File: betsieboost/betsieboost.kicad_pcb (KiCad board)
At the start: 2 copper layers, 35.8 x 14.2 mm, 10 parts, among them J1 Conn_01x03_Male, U1 XL6019E1

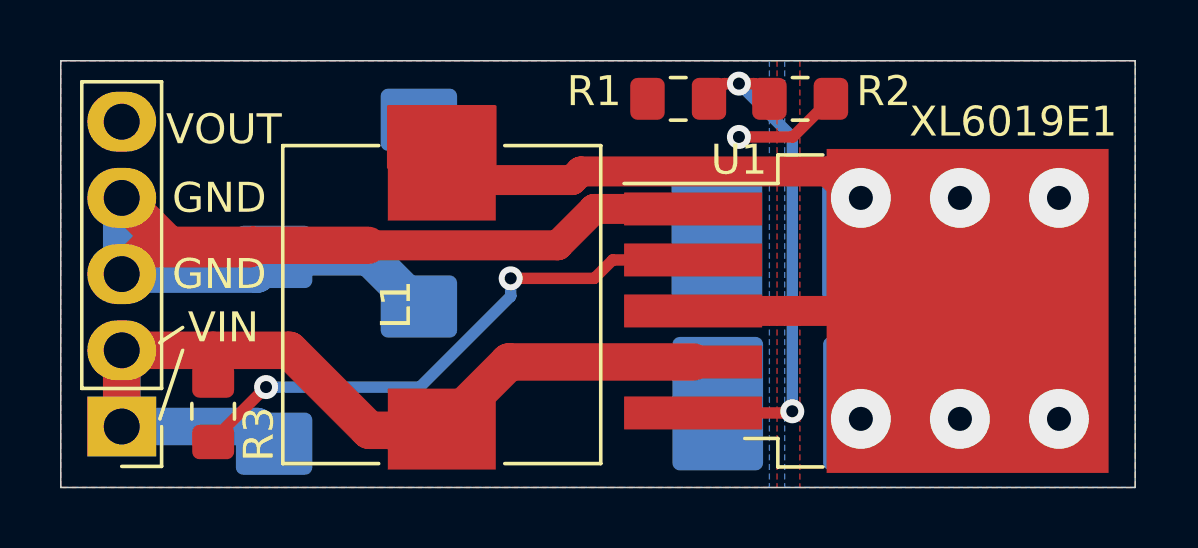
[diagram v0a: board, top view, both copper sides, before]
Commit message: This was an update to add a ceramic cap to the output because those tants do not work well. but I did not respin the board I just hacked it
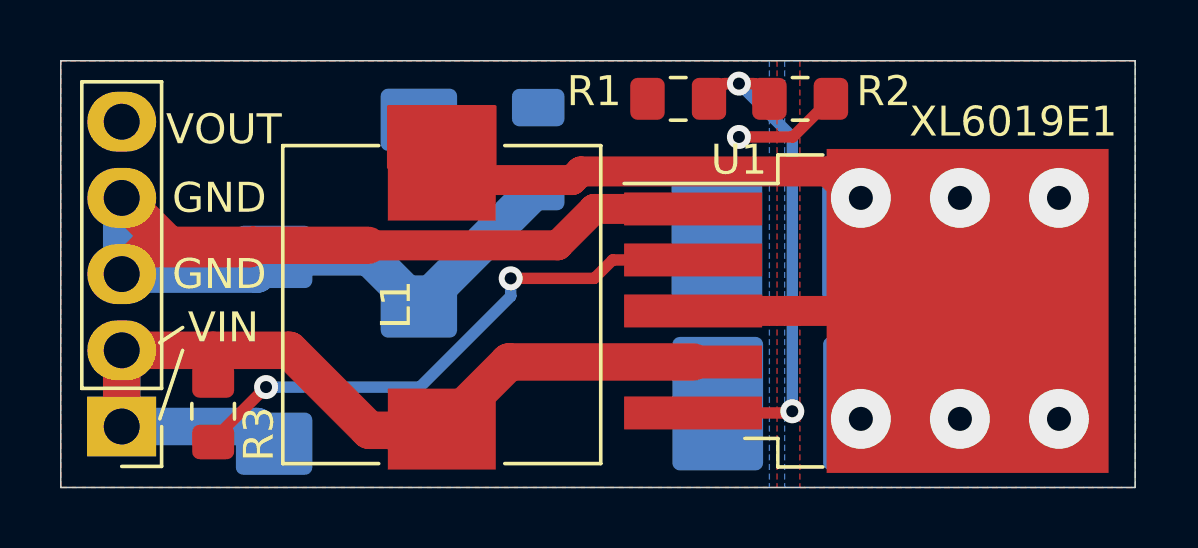
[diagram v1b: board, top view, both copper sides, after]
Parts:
- added C3: 10uF, Capacitor_SMD:C_1206_3216Metric, B.Cu at (130.2, 98.2)
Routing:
- net GND: track 38.4 -> 43.9 mm
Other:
- board text added: "Betsie Boost @markxr 2020"
- board text removed: "Betsie Boost @markxr 2019"
